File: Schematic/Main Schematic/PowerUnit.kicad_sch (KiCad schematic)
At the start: 24 parts, among them J6 USB_B_Micro, U1 MCP1700x-330xxTT

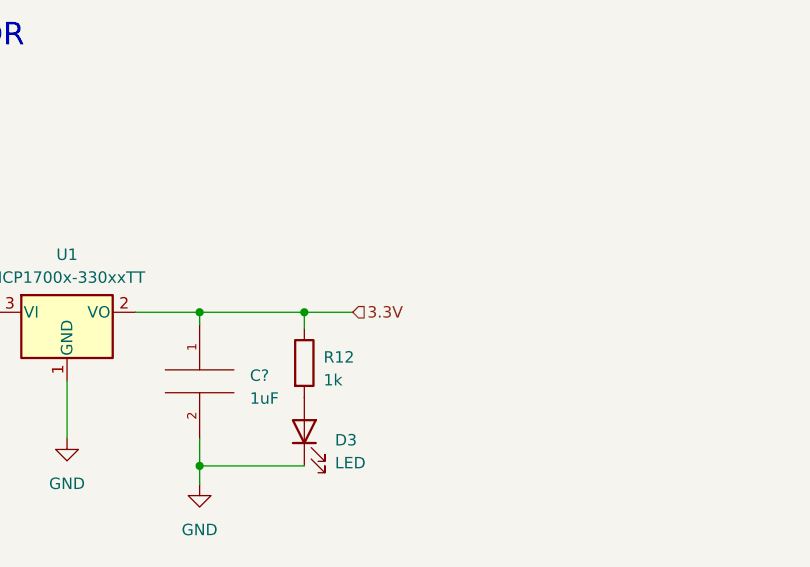
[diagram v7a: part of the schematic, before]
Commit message: added new V regulator
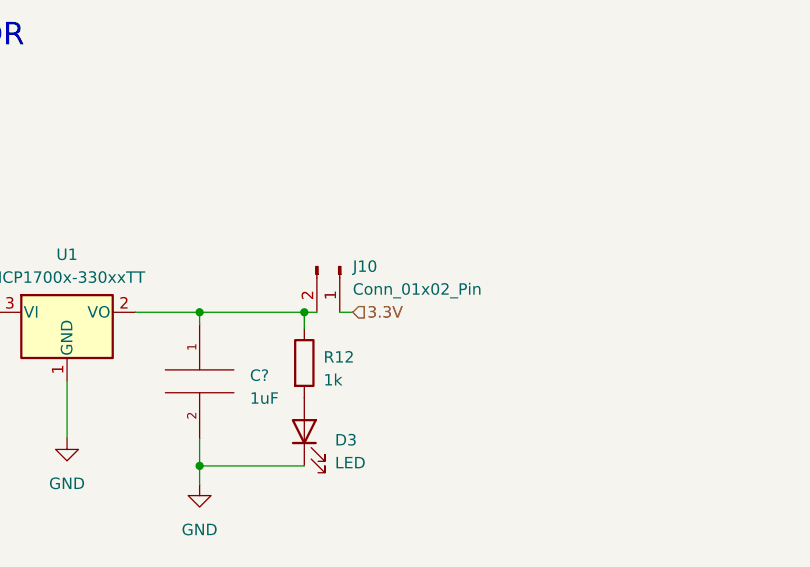
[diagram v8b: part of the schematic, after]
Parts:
- added J10: Conn_01x02_Pin, Connector_PinHeader_2.54mm:PinHeader_1x02_P2.54mm_Vertical, symbol Connector:Conn_01x02_Pin
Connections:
- net 3.3V: now also J10.1 (Pin_1); no longer C?.1, R12.1, U1.2 (VO)
- new net: C?.1, J10.2 (Pin_2), R12.1, U1.2 (VO)
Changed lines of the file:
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@@
+    (stroke (width 0) (type default))
+  )
+  (wire (pts (xy 101.4222 148.59) (xy 102.87 148.59))
     (stroke (width 0) (type default))
   )
@@
     (stroke (width 0) (type default))
   )
-  (wire (pts (xy 97.4852 148.59) (xy 102.87 148.59))
+  (wire (pts (xy 97.4852 148.59) (xy 98.8822 148.59))
     (stroke (width 0) (type default))
   )
@@
         )
       )
+    )
+  )
+  (symbol (lib_id "Connector:Conn_01x02_Pin") (at 101.4222 143.51 270) (unit 1)
+    (in_bom yes) (on_board yes) (dnp no) (fields_autoplaced)
+    (property "Reference" "J10" (at 102.87 143.51 90)
+      (effects (font (size 1.27 1.27)) (justify left))
+    )
+    (property "Value" "Conn_01x02_Pin" (at 102.87 146.05 90)
+      (effects (font (size 1.27 1.27)) (justify left))
+    )
+    (property "Footprint" "Connector_PinHeader_2.54mm:PinHeader_1x02_P2.54mm_Vertical" (at 101.4222 143.51 0)
+      (effects (font (size 1.27 1.27)) hide)
+    )
+    (property "Datasheet" "~" (at 101.4222 143.51 0)
+      (effects (font (size 1.27 1.27)) hide)
+    )
+    (pin "1")
+    (pin "2")
+    (instances
+      (project "Main Schematic"
+        (path "/81c41bad-bb43-41af-b405-18d135a809b1/297def35-fe1a-4185-9e34-6248c2c818f7"
+          (reference "J10") (unit 1)
+        )
+      )
